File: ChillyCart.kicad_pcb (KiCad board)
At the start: 2 copper layers, 51 x 60.7 mm, 74 parts, among them J1 GameBoy_GamePak_DMG-09, J2 USB_C_Receptacle_USB2.0_16P, J3 Micro_SD_Card_Det1, J4 Conn_01x02_Socket, J5 Conn_01x02_Socket, J6 Conn_01x02_Socket, J7 Conn_01x09_Socket, SW1 SW_Push, U1 TXB0108PW, U10 MCP7940N-x/ST, U11 LSM6DS3, U2 TXB0108PW, U3 TXB0108PW, U4 RP2350_80QFN, U5 AMS1117-3.3, U6 W25Q128JVS, U7 DNF, U8 TPS2111A, U9 TXB0108PW, Y1 ABM8-272-T3, Y2 FC-135

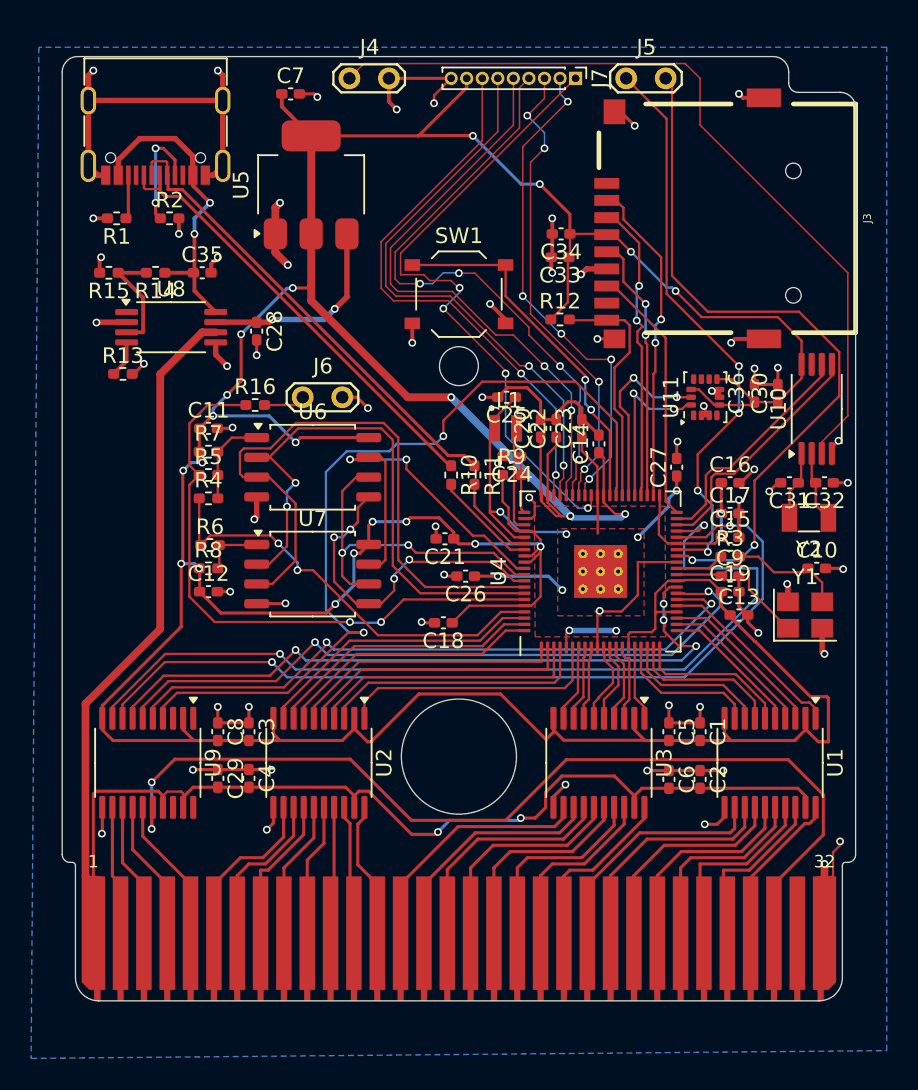
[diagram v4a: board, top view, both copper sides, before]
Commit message: Tidy up silkscreen
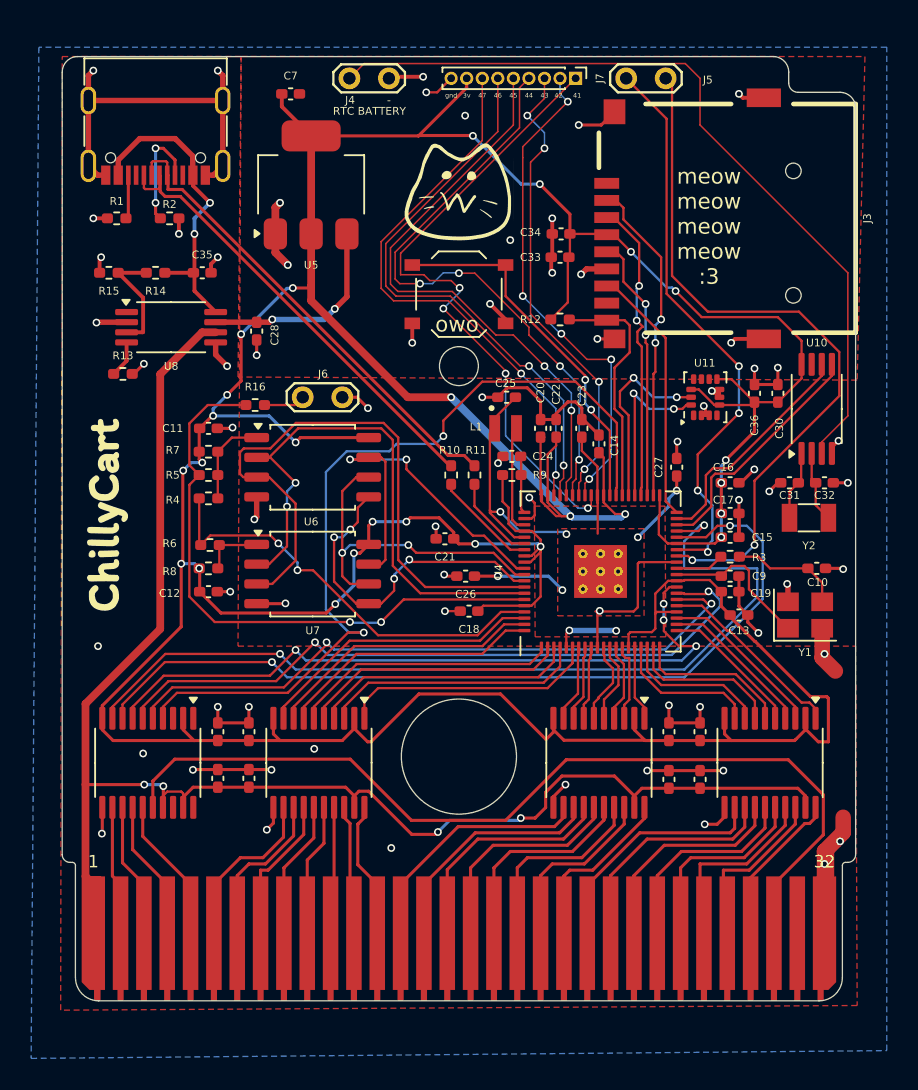
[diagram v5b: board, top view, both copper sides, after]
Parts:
- added G***: LOGO, LOGO, F.Cu at (150.0, 78.7)
- added G***: LOGO, LOGO, F.Cu at (127.5, 99.5)
- added G***: LOGO, LOGO, B.Cu at (164.0, 119.5)
- moved C18 1.81 mm to (150.7, 105.8)
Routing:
- net +3V3: track 317.1 -> 321.2 mm, vias 26 -> 28
- net GND: track 138.1 -> 142.2 mm, vias 63 -> 68
- net +5V_CART: track 100.9 -> 96.9 mm, vias 2 -> 4
- net RST: track 59.4 -> 56.7 mm, vias 2 -> 0
- net RP_ADDR7: track 17.1 -> 16.5 mm
- net RP_ADDR4: track 17.5 -> 17.0 mm
- net RP_ADDR5: track 17.5 -> 17.0 mm
- added copper zone on F.Cu, net GND
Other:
- board text added: "-"
- board text added: "3v"
- board text added: "41"
- board text added: "42"
- board text added: "43"
- board text added: "44"
- board text added: "45"
- board text added: "46"
- board text added: "47"
- board text added: "ChillyCart v0 https://github.com/ChillyGB"
- board text added: "RTC BATTERY"
- board text added: "gnd"
- board text added: "meow meow meow meow :3"
- board text added: "owo"
